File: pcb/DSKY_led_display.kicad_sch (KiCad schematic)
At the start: 237 parts, among them J1 105133-0001, J2 3221-10-0300-00-TR, J3 TSM-104-01-L-SV, SW1 KMR241NG, U1 AP2204K-3.3, U2 LP5036, U3 LP5036, U4 LP5036, U5 LP5036, U6 ATSAMD21E18A-A, U7 LP5036, U8 LP5036, U9 TCA9543ADR

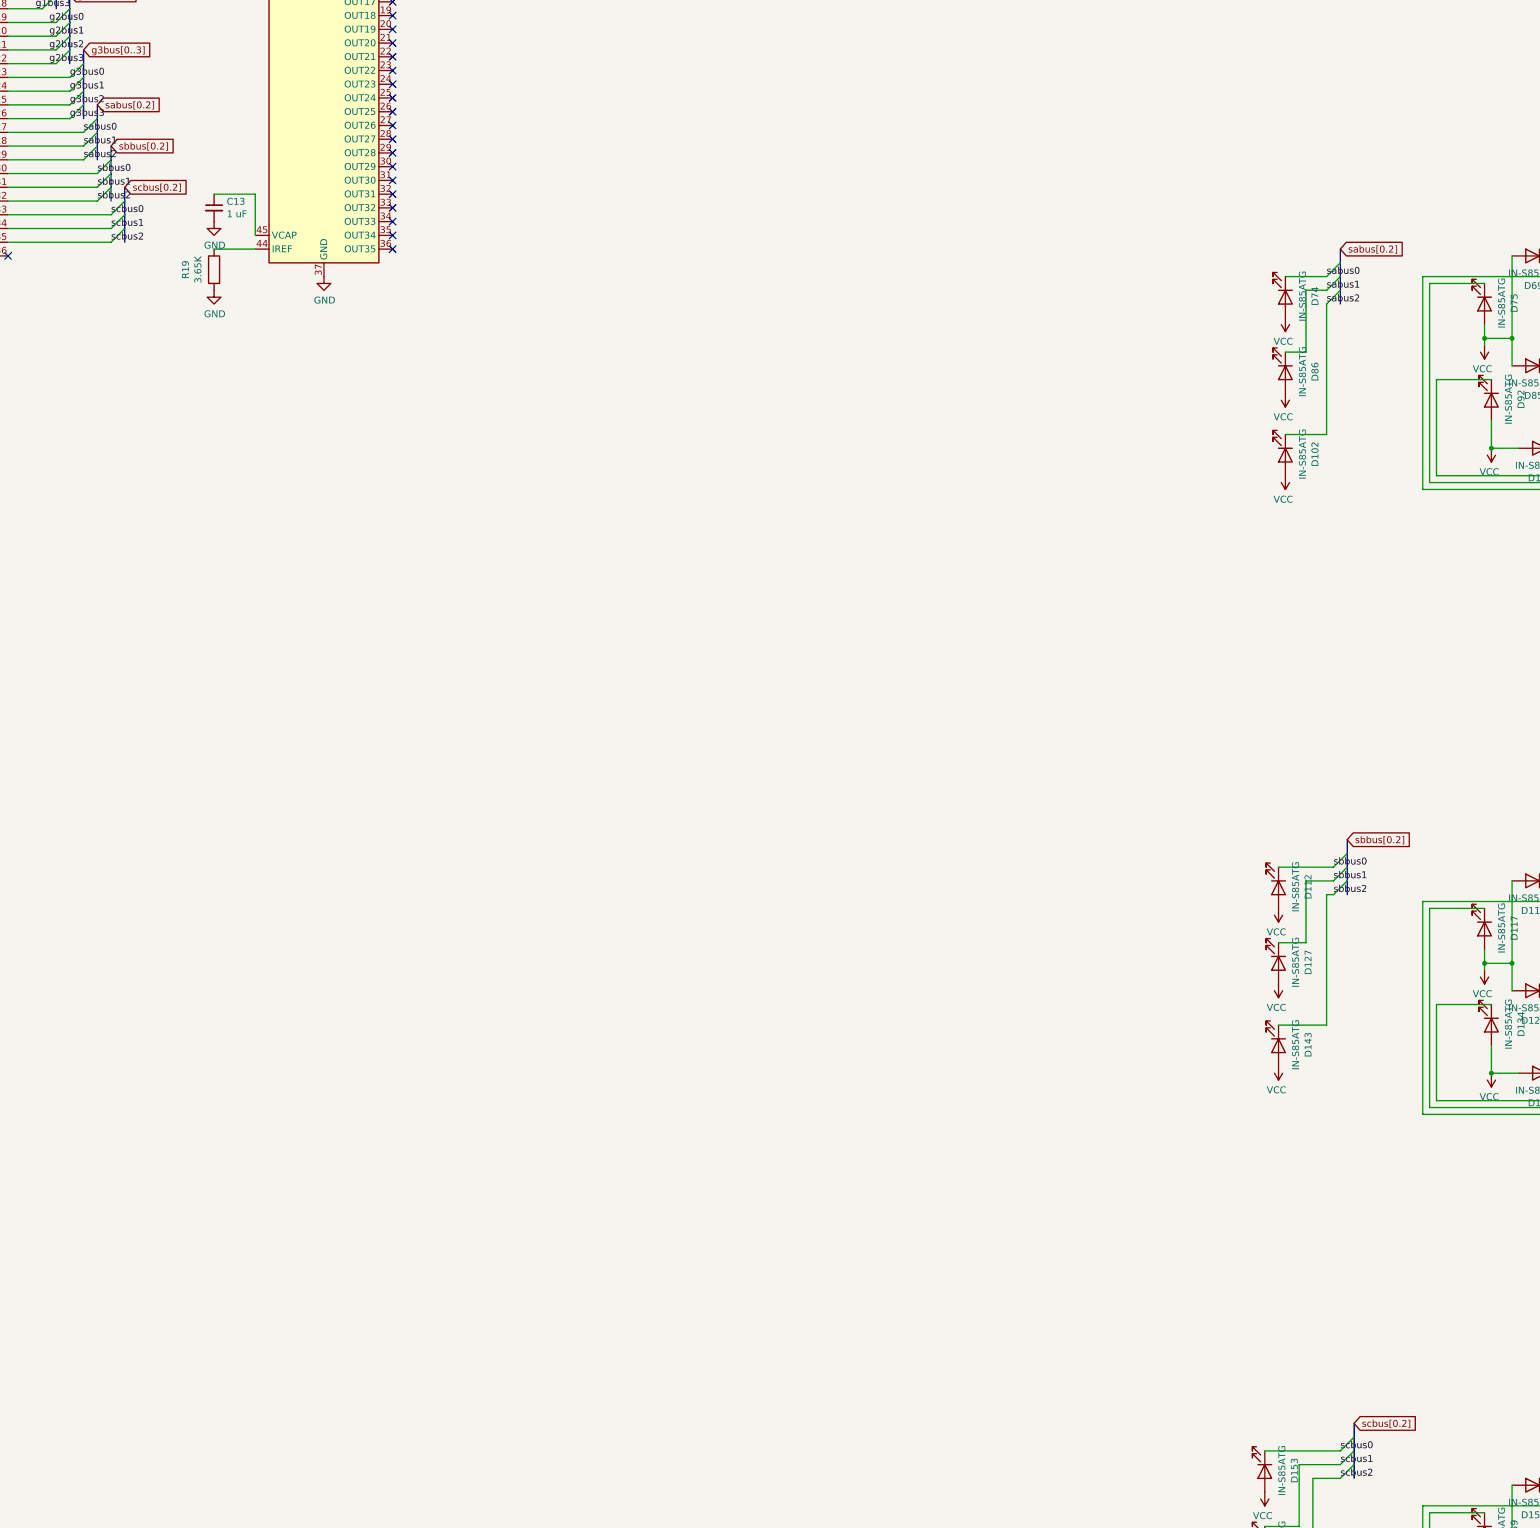
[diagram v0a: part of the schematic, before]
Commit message: Update owing to KiCad V7 being fussier about bus definitions
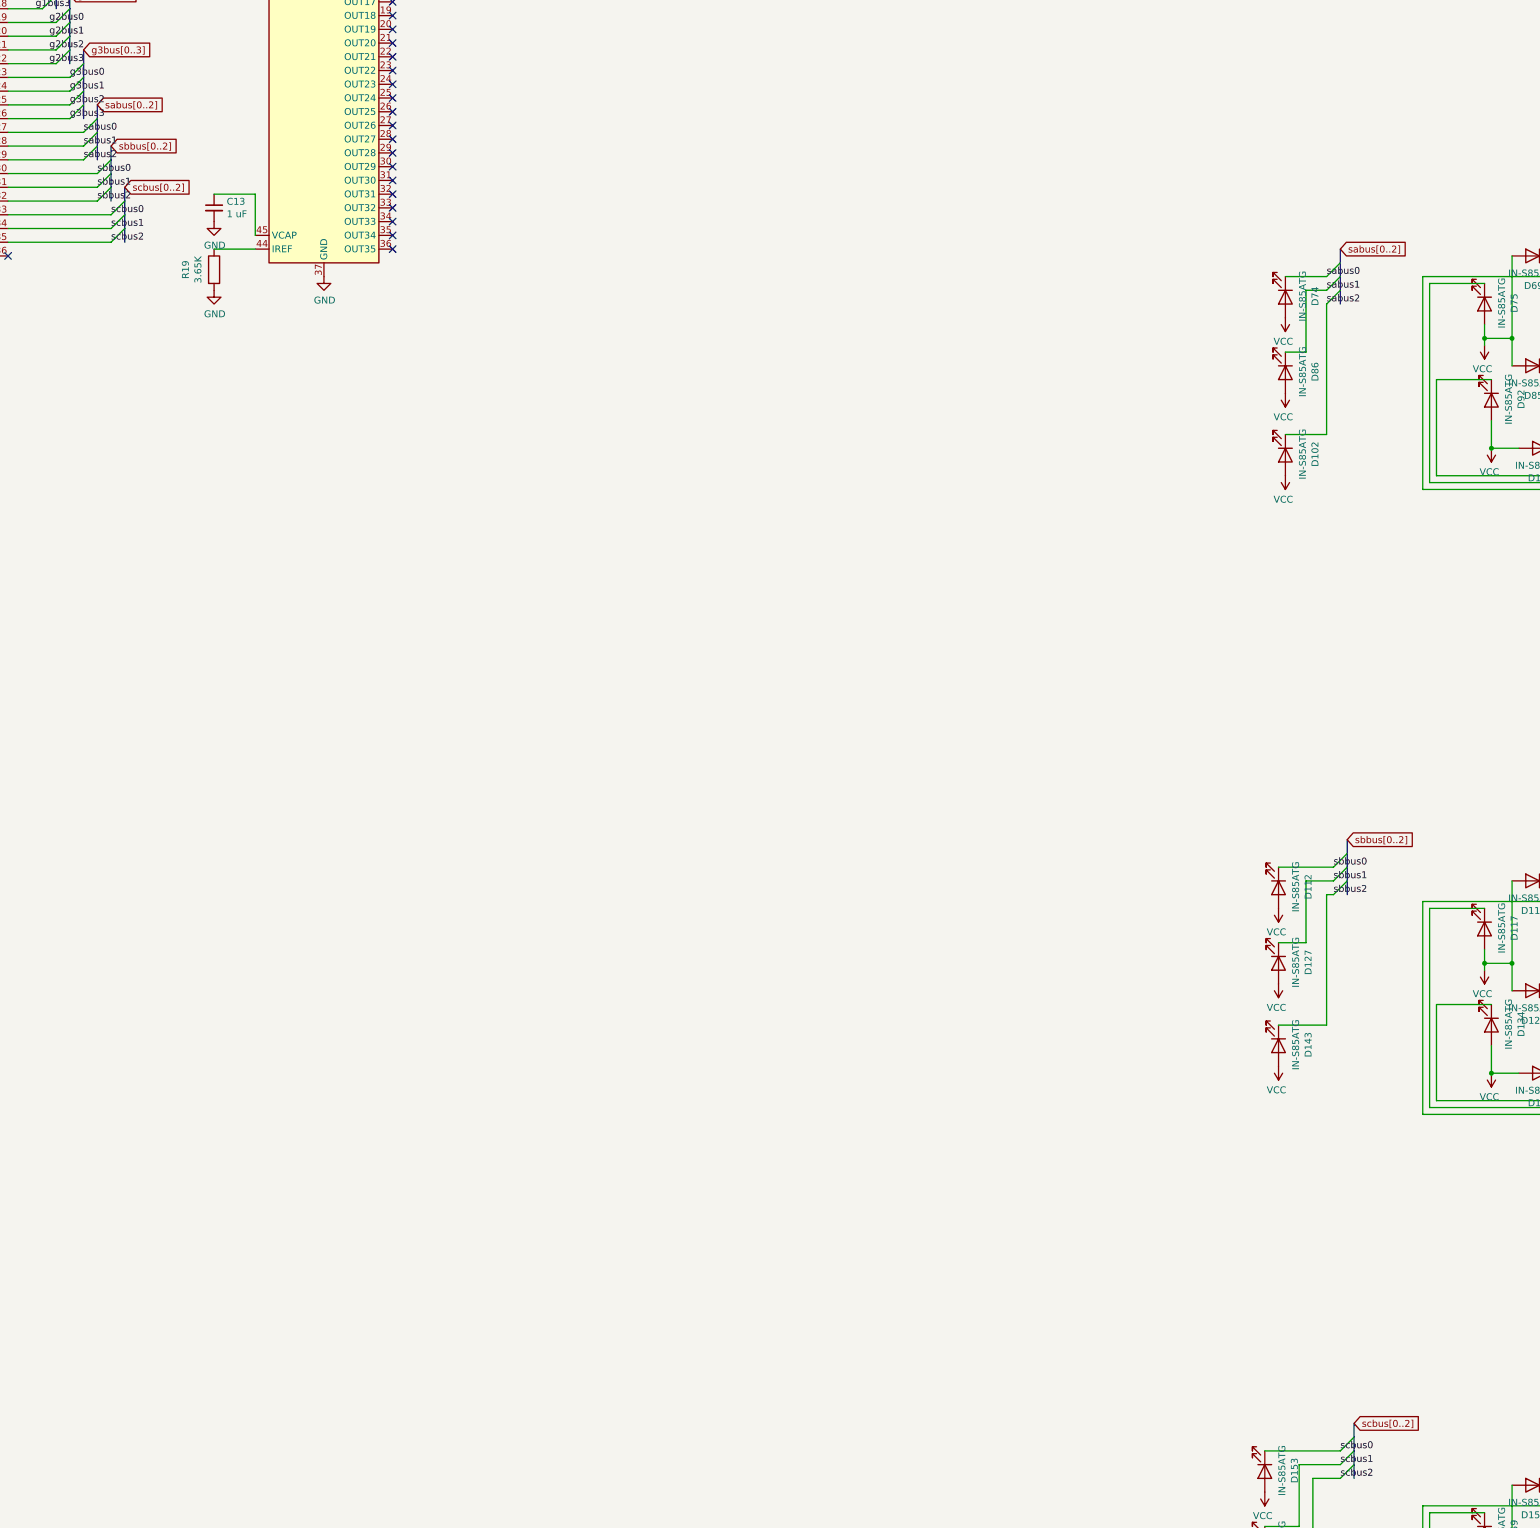
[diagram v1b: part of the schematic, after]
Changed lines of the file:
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@@
     (stroke (width 0) (type default))
   )
+  (bus (pts (xy 215.9 278.13) (xy 215.9 280.67))
+    (stroke (width 0) (type default))
+  )
   (bus (pts (xy 199.39 118.11) (xy 199.39 120.65))
     (stroke (width 0) (type default))
@@
     (stroke (width 0) (type default))
   )
-  (bus (pts (xy 215.9 278.13) (xy 215.9 280.67))
-    (stroke (width 0) (type default))
-  )
   (wire (pts (xy 203.2 250.19) (xy 199.39 250.19))
     (stroke (width 0) (type default))
@@
     )
   )
-  (global_label "scbus[0.2]" (shape input) (at 220.98 293.37 0)
+  (global_label "scbus[0..2]" (shape input) (at 220.98 293.37 0)
     (effects (font (size 1.27 1.27)) (justify left))
     (property "Intersheetrefs" "${INTERSHEET_REFS}" (at 220.98 293.37 0)
@@
     )
   )
-  (global_label "scbus[0.2]" (shape input) (at 448.31 521.97 0)
+  (global_label "scbus[0..2]" (shape input) (at 448.31 521.97 0)
     (effects (font (size 1.27 1.27)) (justify left))
     (property "Intersheetrefs" "${INTERSHEET_REFS}" (at 448.31 521.97 0)
@@
     )
   )
-  (global_label "sabus[0.2]" (shape input) (at 445.77 304.8 0)
+  (global_label "sabus[0..2]" (shape input) (at 445.77 304.8 0)
     (effects (font (size 1.27 1.27)) (justify left))
     (property "Intersheetrefs" "${INTERSHEET_REFS}" (at 445.77 304.8 0)
@@
     )
   )
-  (global_label "sbbus[0.2]" (shape input) (at 218.44 285.75 0)
+  (global_label "sbbus[0..2]" (shape input) (at 218.44 285.75 0)
     (effects (font (size 1.27 1.27)) (justify left))
     (property "Intersheetrefs" "${INTERSHEET_REFS}" (at 218.44 285.75 0)
@@
     )
   )
-  (global_label "sbbus[0.2]" (shape input) (at 447.04 414.02 0)
+  (global_label "sbbus[0..2]" (shape input) (at 447.04 414.02 0)
     (effects (font (size 1.27 1.27)) (justify left))
     (property "Intersheetrefs" "${INTERSHEET_REFS}" (at 447.04 414.02 0)
@@
     )
   )
-  (global_label "sabus[0.2]" (shape input) (at 215.9 278.13 0)
+  (global_label "sabus[0..2]" (shape input) (at 215.9 278.13 0)
     (effects (font (size 1.27 1.27)) (justify left))
     (property "Intersheetrefs" "${INTERSHEET_REFS}" (at 215.9 278.13 0)

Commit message: V6 and V7 PCB
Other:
- note added: "LED Power Connector"

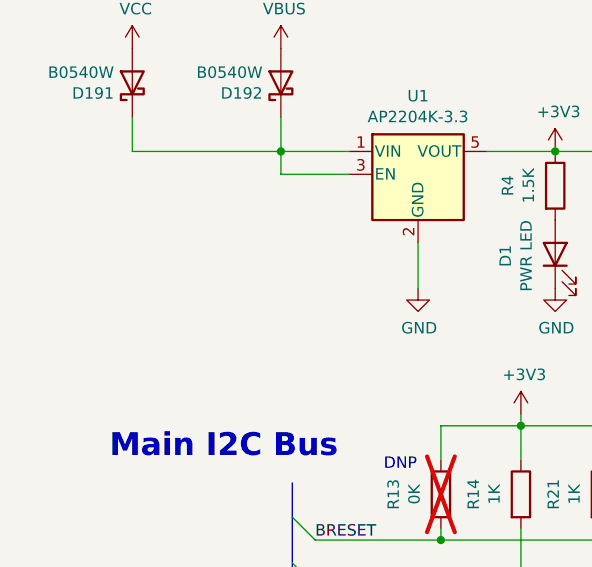
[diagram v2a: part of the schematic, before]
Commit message: Add SIngle Power Source mod notes
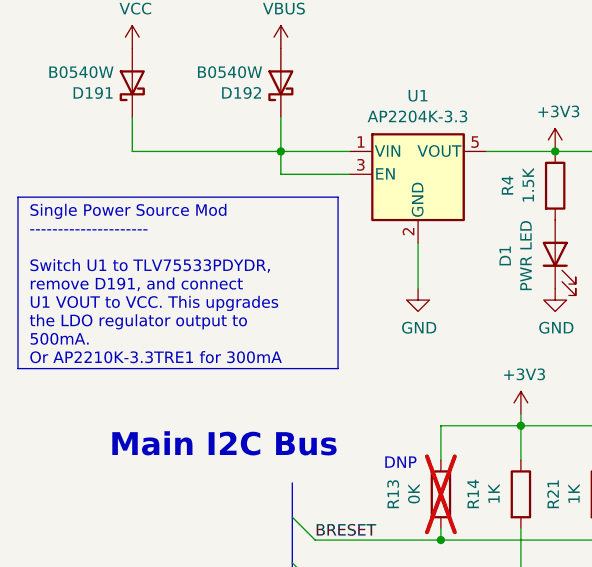
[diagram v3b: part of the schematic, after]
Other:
- note added: "Single Power Source Mod --------------------- Switch U1 to TLV75533PDYDR, remove D191, and connect U1 VOUT to VCC. This upgrades the LDO regulator output to 500mA. Or AP2210K-3.3TRE1 for 300mA"
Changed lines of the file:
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@@
 		(comment 1 "https://github.com/rrainey/DSKY-display-indicator")
+	)
+	(rectangle
+		(start 15.24 74.93)
+		(end 50.8 93.98)
+		(stroke
+			(width 0)
+			(type default)
+		)
+		(fill
+			(type none)
+		)
 	)
 	(text "I2C Bus 1"
@@
 		)
 	)
+	(text "Single Power Source Mod\n---------------------\n\nSwitch U1 to TLV75533PDYDR, \nremove D191, and connect \nU1 VOUT to VCC. This upgrades \nthe LDO regulator output to \n500mA.\nOr AP2210K-3.3TRE1 for 300mA"
+		(exclude_from_sim no)
+		(at 16.51 84.836 0)
+		(effects
+			(font
+				(size 1.27 1.27)
+			)
+			(justify left)
+		)
+	)

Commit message: update notes
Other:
- note added: "VCC is an externl 3.3V source. It powers the LED array, 6 LP5036 LED drivers, and two I2C busses. +3V3 powers the SAMD21 MCU and the main I2C bus. VBUS is the incoming 5V USB power source"
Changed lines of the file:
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@@
 	)
 	(rectangle
+		(start 100.33 19.05)
+		(end 165.1 31.75)
+		(stroke
+			(width 0)
+			(type default)
+		)
+		(fill
+			(type none)
+		)
+	)
+	(rectangle
 		(start 15.24 74.93)
-		(end 50.8 93.98)
+		(end 50.8 95.25)
 		(stroke
 			(width 0)
@@
 		)
 	)
+	(text "VCC   is an externl 3.3V source. It powers the LED array, \n       6 LP5036 LED drivers, and two I2C busses.\n+3V3 powers the SAMD21 MCU and the main I2C bus.\nVBUS is the incoming 5V USB power source"
+		(exclude_from_sim no)
+		(at 104.14 25.146 0)
+		(effects
+			(font
+				(size 1.27 1.27)
+			)
+			(justify left)
+		)
+	)
 	(text "USB Micro-B"
 		(exclude_from_sim no)
@@
 	(wire
 		(pts
+			(xy 74.93 58.42) (xy 74.93 69.85)
+		)
+		(stroke
+			(width 0)
+			(type default)
+		)
+	)
+	(wire
+		(pts
 			(xy 594.36 189.23) (xy 633.73 189.23)
 		)
@@
 	(symbol
 		(lib_id "power:+3V3")
-		(at 74.93 69.85 0)
+		(at 74.93 58.42 0)
 		(unit 1)
 		(exclude_from_sim no)
@@
 		(dnp no)
 		(property "Reference" "#PWR012"
-			(at 74.93 73.66 0)
+			(at 74.93 62.23 0)
 			(effects
 				(font
@@
 		)
 		(property "Value" "+3V3"
-			(at 75.311 65.4558 0)
+			(at 75.311 54.0258 0)
 			(effects
 				(font
@@
 		)
 		(property "Footprint" ""
-			(at 74.93 69.85 0)
+			(at 74.93 58.42 0)
 			(effects
 				(font
@@
 		)
 		(property "Datasheet" ""
-			(at 74.93 69.85 0)
+			(at 74.93 58.42 0)
 			(effects
 				(font
@@
 		)
 		(property "Description" ""
-			(at 74.93 69.85 0)
+			(at 74.93 58.42 0)
 			(effects
 				(font
